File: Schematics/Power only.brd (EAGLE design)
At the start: 100 x 80 mm, 9 parts, among them IC1 OPA548T, IC2 OPA2336P, U1 MCP4822-E/P

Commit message: added some pluggery
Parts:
- added C2, C3: 0.1µF, microbuilder:0805
- added J1, J2: TERMBLOCK_1X2-3.5MM, microbuilder:1X2-3.5MM
- added JP1, JP2: (no value), microbuilder:1X06_ROUND_70
- added R10, R11, R12, R13, R5, R6, R7, R8: 10K, microbuilder:0805
- added R14, R9: 0.1/1% (PT2512FK-070R1L), microbuilder:2512
- added SJ1, SJ2, SJ3, SJ4: (no value), microbuilder:SOLDERJUMPER_REFLOW_NOPASTE
- added U2, U3: INA219BIDCNT, microbuilder:SOT23-8
- added X1: (no value), con-phoenix-254:2POL254
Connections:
- removed net VCELL: IC1.6, R1.2
- new net GND: C2.2, C3.2, JP1.2, JP2.2, R10.1, R11.1, R5.1, R6.1, U2.3, U3.3
- new net N$10: R10.2, SJ3.2, U3.7
- new net N$5: R6.2, SJ2.2, U2.8
- new net N$7: R5.2, SJ1.2, U2.7
- new net N$9: R11.2, SJ4.2, U3.8
- new net SCL: JP1.3, JP2.3, R12.1, R7.1, U2.5, U3.5
- new net SDA: JP1.4, JP2.4, R13.1, R8.1, U2.6, U3.6
- new net VIN+: IC1.6, J1.2, J2.2, JP1.6, JP2.6, R1.2, R14.2, R9.2, U2.1, U3.1
- new net VIN-: J1.1, J2.1, JP1.5, JP2.5, R14.1, R9.1, U2.2, U3.2, X1.1, X1.2
- net VCC: now also C2.1, C3.1, JP1.1, JP2.1, R12.2, R13.2, R7.2, R8.2, SJ1.1, SJ2.1, SJ3.1, SJ4.1, U2.4, U3.4

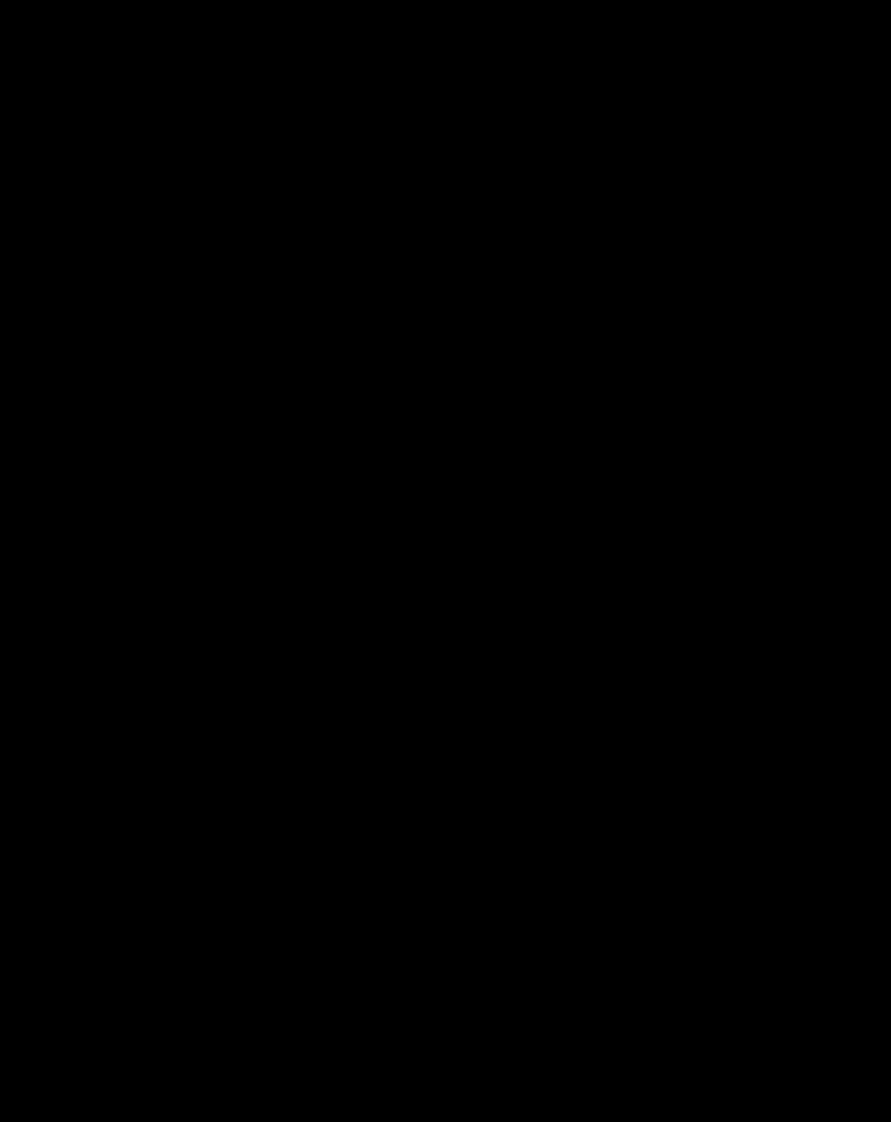
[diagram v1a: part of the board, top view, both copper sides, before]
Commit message: Temp sense and H bridge
plug for temp sensor wiring for H bridge to arduino
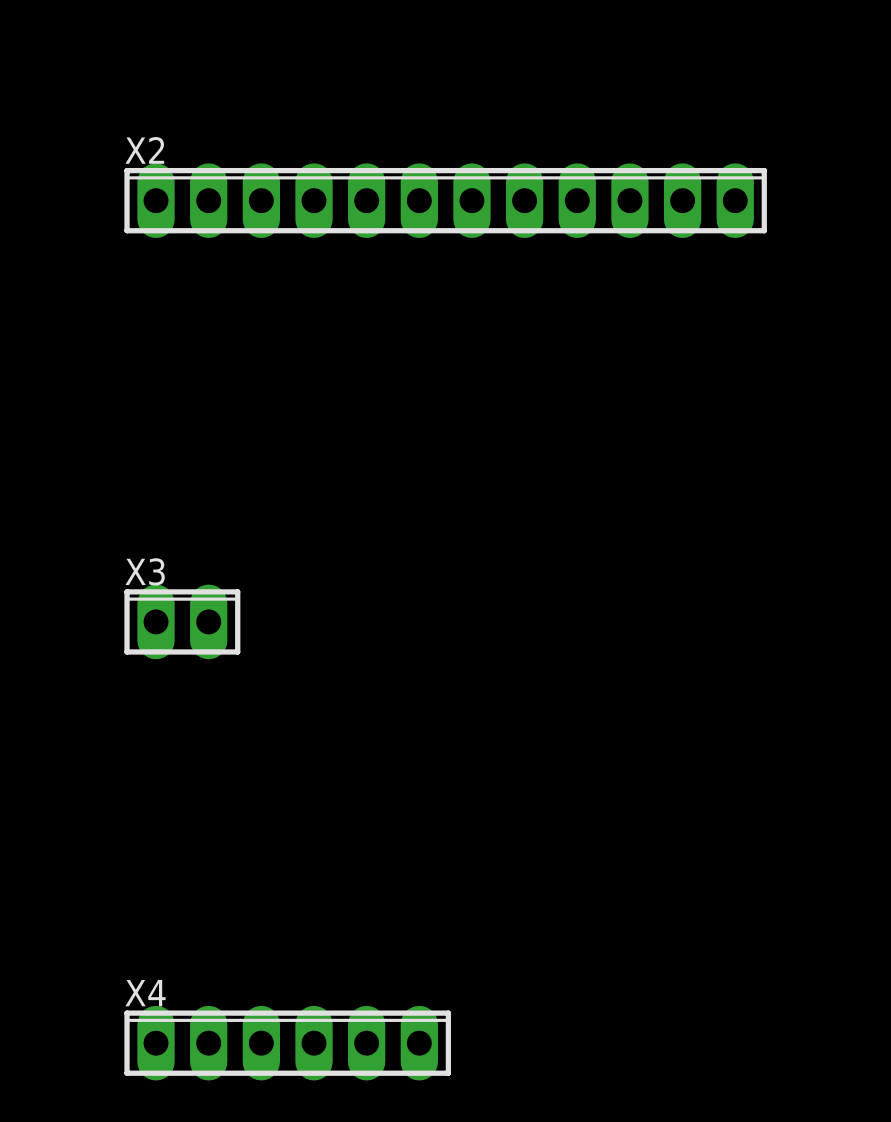
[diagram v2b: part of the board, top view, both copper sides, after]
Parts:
- added X2: (no value), con-phoenix-254:12POL254
- added X3: 13, con-phoenix-254:2POL254
- added X4: (no value), con-phoenix-254:6POL254
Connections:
- new net N$11: X2.2
- new net N$13: X2.4
- new net N$15: X2.6
- new net N$16: X2.7
- new net N$17: X2.8
- new net N$18: X2.9
- new net N$19: X2.10
- new net N$21: X2.12
- new net N$22: X3.2
- new net N$8: J1.2, R9.2, U2.1, X4.6
- net GNDA: now also X4.4
- net VIN+: now also X4.3, X4.5; no longer J1.2, R9.2, U2.1
